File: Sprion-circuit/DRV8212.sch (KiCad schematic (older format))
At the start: 19 parts, among them U1 LM358, U2 LM358

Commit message: デスクトップいくよーーー
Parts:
- removed U1, U2: LM358, symbol Amplifier_Operational:LM358
- added C14: 0.1u, symbol Device:C
- added IC3, IC4: AD8601, symbol Sprion-circuit:AD8601
- C3: value 0.1 -> 0.1u
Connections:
- wire segments 45 -> 42
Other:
- moved on the sheet: C1, C2, R1, R2, R4, R5

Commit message: Push, Push, Push
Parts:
- C1, C2: value 0.1 -> 0.1u
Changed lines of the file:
@@
 	0    1    1    0
 $EndComp
-Text HLabel 3800 1950 2    50   Input ~ 0
+Text HLabel 3800 1950 2    50   Output ~ 0
 MD1_OUT1
-Text HLabel 3800 2250 2    50   Input ~ 0
+Text HLabel 3800 2250 2    50   Output ~ 0
 MD1_OUT2
 $Comp
@@
 	1    0    0    -1
 $EndComp
-Text HLabel 4850 3200 2    50   Input ~ 0
+Text HLabel 4850 3200 2    50   Output ~ 0
 MD1_CS
 $Comp
@@
 P 4300 4300
 F 0 "C1" V 4048 4300 50  0000 C CNN
-F 1 "0.1" V 4139 4300 50  0000 C CNN
+F 1 "0.1u" V 4139 4300 50  0000 C CNN
 F 2 "" H 4338 4150 50  0001 C CNN
 F 3 "~" H 4300 4300 50  0001 C CNN
@@
 	0    1    1    0
 $EndComp
-Text HLabel 3800 4700 2    50   Input ~ 0
+Text HLabel 3800 4700 2    50   Output ~ 0
 MD2_OUT1
-Text HLabel 3800 5000 2    50   Input ~ 0
+Text HLabel 3800 5000 2    50   Output ~ 0
 MD2_OUT2
 $Comp
@@
 	1    0    0    -1
 $EndComp
-Text HLabel 4850 5950 2    50   Input ~ 0
+Text HLabel 4850 5950 2    50   Output ~ 0
 MD2_CS
 $Comp
@@
 P 4300 7050
 F 0 "C2" V 4048 7050 50  0000 C CNN
-F 1 "0.1" V 4139 7050 50  0000 C CNN
+F 1 "0.1u" V 4139 7050 50  0000 C CNN
 F 2 "" H 4338 6900 50  0001 C CNN
 F 3 "~" H 4300 7050 50  0001 C CNN
@@
 	0    1    1    0
 $EndComp
-Text HLabel 8350 1950 2    50   Input ~ 0
+Text HLabel 8350 1950 2    50   Output ~ 0
 MD_SUC_OUT1
-Text HLabel 8350 2250 2    50   Input ~ 0
+Text HLabel 8350 2250 2    50   Output ~ 0
 MD_SUC_OUT2
 $Comp

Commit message: :fix　いろいろ
後で書きます
とりあえず寝ます
許してください
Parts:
- added J?: Conn_01x02_Female, symbol Connector:Conn_01x02_Female
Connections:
- net MD_SUC_OUT1: no longer names the net of MD3.6 (OUT1)
- net MD_SUC_OUT1: now also J?.1 (Pin_1)
- net MD_SUC_OUT2: no longer names the net of MD3.4 (OUT2)
- net MD_SUC_OUT2: now also J?.2 (Pin_2)
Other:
- moved on the sheet: C6, MD3
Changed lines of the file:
@@
 $Descr A4 11693 8268
 encoding utf-8
-Sheet 2 5
+Sheet 2 6
 Title ""
 Date ""
@@
 Wire Wire Line
 	3900 4000 3900 4300
-Text Notes 5600 3550 0    50   ~ 0
-Amplification rate:51\nTransfer function:V_out=0.51*I_s\nCut off frequency:796Hz
 $Comp
 L Sprion-circuit:DRV8212_DRL MD2
@@
 	3900 6750 3900 7050
 $Comp
-L Sprion-circuit:DRV8212_DRL MD3
-U 1 1 60F210D1
-P 8000 2100
-F 0 "MD3" H 8000 2515 50  0000 C CNN
-F 1 "DRV8212_DRL" H 8000 2424 50  0000 C CNN
-F 2 "" H 8000 2100 50  0001 C CNN
-F 3 "" H 8000 2100 50  0001 C CNN
-	1    8000 2100
-	1    0    0    -1
-$EndComp
-Text HLabel 7650 1950 0    50   Input ~ 0
-MD_SUC_IN1
-Text HLabel 7650 2100 0    50   Input ~ 0
-MD_SUC_IN2
-$Comp
 L power:+BATT #PWR0112
 U 1 1 60F210D9
-P 9200 2100
-F 0 "#PWR0112" H 9200 1950 50  0001 C CNN
-F 1 "+BATT" V 9215 2228 50  0000 L CNN
-F 2 "" H 9200 2100 50  0001 C CNN
-F 3 "" H 9200 2100 50  0001 C CNN
-	1    9200 2100
-	0    1    1    0
-$EndComp
-Text HLabel 8350 1950 2    50   Output ~ 0
-MD_SUC_OUT1
-Text HLabel 8350 2250 2    50   Output ~ 0
-MD_SUC_OUT2
+P 8350 1600
+F 0 "#PWR0112" H 8350 1450 50  0001 C CNN
+F 1 "+BATT" V 8365 1728 50  0000 L CNN
+F 2 "" H 8350 1600 50  0001 C CNN
+F 3 "" H 8350 1600 50  0001 C CNN
+	1    8350 1600
+	1    0    0    -1
+$EndComp
 $Comp
 L power:GND #PWR0113
 U 1 1 60F210E1
-P 8950 2400
-F 0 "#PWR0113" H 8950 2150 50  0001 C CNN
-F 1 "GND" H 8955 2227 50  0000 C CNN
-F 2 "" H 8950 2400 50  0001 C CNN
-F 3 "" H 8950 2400 50  0001 C CNN
-	1    8950 2400
-	1    0    0    -1
-$EndComp
-$Comp
-L Device:C C6
-U 1 1 60F210E7
-P 8950 2250
-F 0 "C6" H 9065 2296 50  0000 L CNN
-F 1 "0.1u" H 9065 2205 50  0000 L CNN
-F 2 "" H 8988 2100 50  0001 C CNN
-F 3 "~" H 8950 2250 50  0001 C CNN
-	1    8950 2250
-	1    0    0    -1
-$EndComp
-Wire Wire Line
-	8350 2100 8950 2100
-Connection ~ 8950 2100
-Wire Wire Line
-	8950 2100 9200 2100
-$Comp
-L power:GND #PWR0114
-U 1 1 60F21B92
-P 7650 2250
-F 0 "#PWR0114" H 7650 2000 50  0001 C CNN
-F 1 "GND" H 7655 2077 50  0000 C CNN
-F 2 "" H 7650 2250 50  0001 C CNN
-F 3 "" H 7650 2250 50  0001 C CNN
-	1    7650 2250
+P 8950 1850
+F 0 "#PWR0113" H 8950 1600 50  0001 C CNN
+F 1 "GND" H 8955 1677 50  0000 C CNN
+F 2 "" H 8950 1850 50  0001 C CNN
+F 3 "" H 8950 1850 50  0001 C CNN
+	1    8950 1850
 	1    0    0    -1
 $EndComp
@@
 	4200 5650 4350 5650
 Connection ~ 4200 5650
+$Comp
+L power:GND #PWR0114
+U 1 1 60F21B92
+P 7450 2600
+F 0 "#PWR0114" H 7450 2350 50  0001 C CNN
+F 1 "GND" H 7455 2427 50  0000 C CNN
+F 2 "" H 7450 2600 50  0001 C CNN
+F 3 "" H 7450 2600 50  0001 C CNN
+	1    7450 2600
+	1    0    0    -1
+$EndComp
+Text HLabel 7450 2450 0    50   Input ~ 0
+MD_SUC_IN2
+Text HLabel 7450 2300 0    50   Input ~ 0
+MD_SUC_IN1
+$Comp
+L Sprion-circuit:DRV8212_DRL MD3
+U 1 1 60F210D1
+P 7800 2450
+F 0 "MD3" H 7800 2865 50  0000 C CNN
+F 1 "DRV8212_DRL" H 7800 2774 50  0000 C CNN
+F 2 "" H 7800 2450 50  0001 C CNN
+F 3 "" H 7800 2450 50  0001 C CNN
+	1    7800 2450
+	1    0    0    -1
+$EndComp
+Text Notes 5600 3550 0    50   ~ 0
+Amplification rate:51\nTransfer function:V_out=0.51*I_s\nCut off frequency:796Hz
+$Comp
+L Connector:Conn_01x02_Female J?
+U 1 1 61A82ABA
+P 10000 2300
+F 0 "J?" H 10028 2276 50  0000 L CNN
+F 1 "Conn_01x02_Female" H 10028 2185 50  0000 L CNN
+F 2 "" H 10000 2300 50  0001 C CNN
+F 3 "~" H 10000 2300 50  0001 C CNN
+	1    10000 2300
+	1    0    0    -1
+$EndComp
+Wire Wire Line
+	8150 2300 9800 2300
+Wire Wire Line
+	8150 2600 9800 2600
+Wire Wire Line
+	9800 2600 9800 2400
+Wire Wire Line
+	8350 2450 8150 2450
+Wire Wire Line
+	8350 1600 8350 1850
+$Comp
+L Device:C C6
+U 1 1 60F210E7
+P 8700 1850
+F 0 "C6" H 8815 1896 50  0000 L CNN
+F 1 "0.1u" H 8815 1805 50  0000 L CNN
+F 2 "" H 8738 1700 50  0001 C CNN
+F 3 "~" H 8700 1850 50  0001 C CNN
+	1    8700 1850
+	0    -1   -1   0
+$EndComp
+Wire Wire Line
+	8550 1850 8350 1850
+Connection ~ 8350 1850
+Wire Wire Line
+	8350 1850 8350 2450
+Wire Wire Line
+	8850 1850 8950 1850
 $EndSCHEMATC

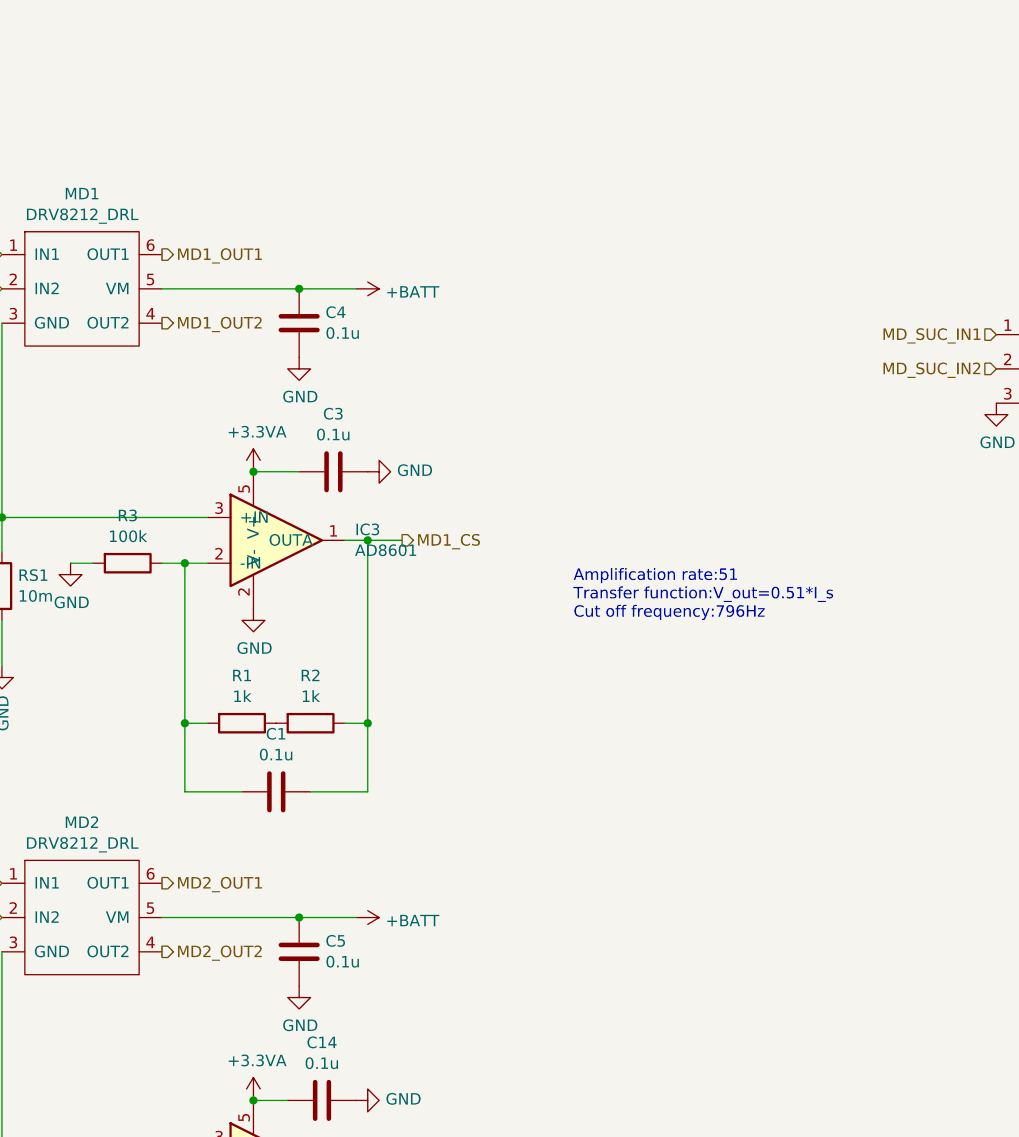
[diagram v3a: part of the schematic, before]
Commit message: fix: MD周り,タイマー割り当て
MDの書き方を変えた
タイマー割り当てを再構成、対称性・高性能タイマーをどうするかみたいなとこ
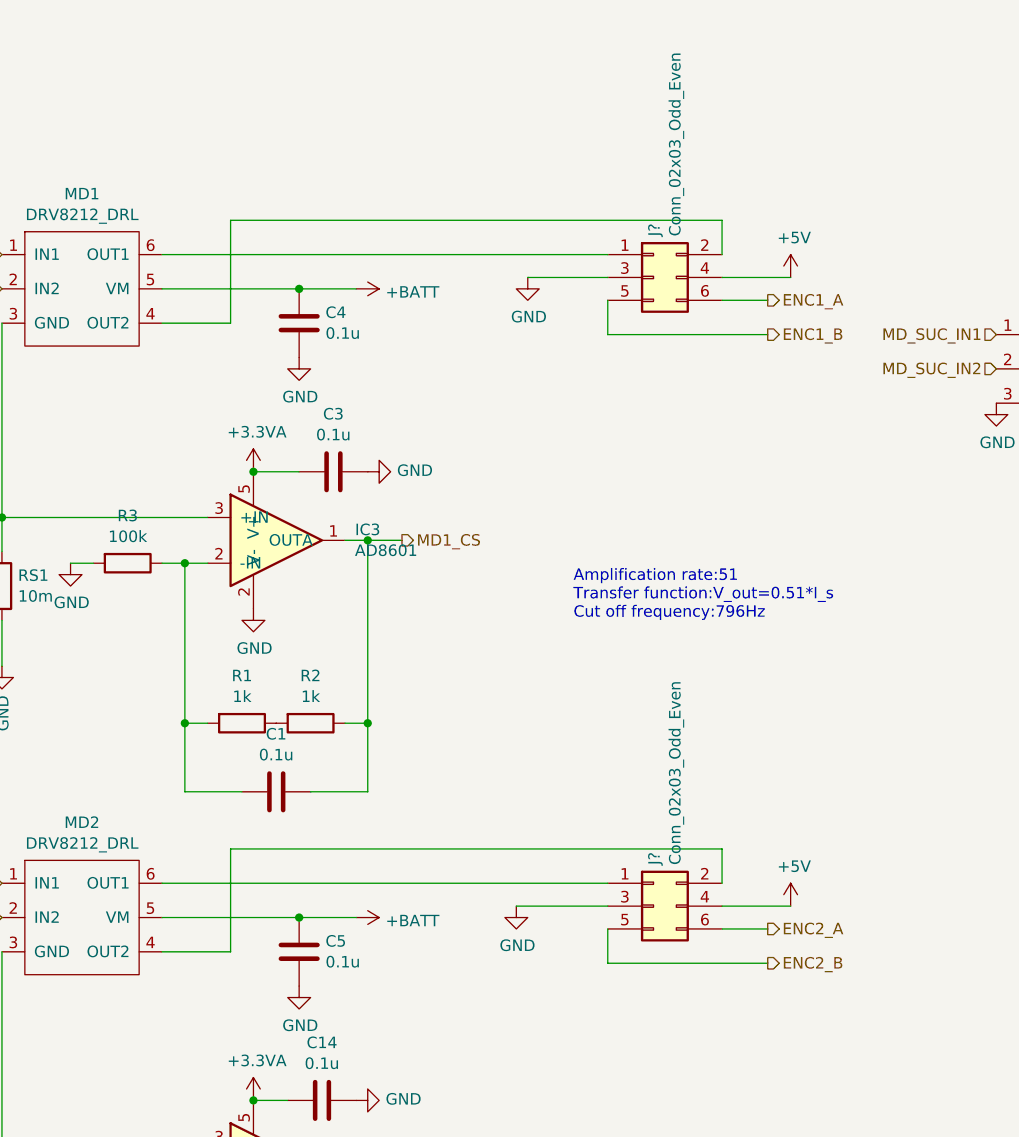
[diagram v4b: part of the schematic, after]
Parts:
- added J? (x2): Conn_02x03_Odd_Even, symbol Connector_Generic:Conn_02x03_Odd_Even
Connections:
- net GND: now also J?.3 (Pin_3), J?.3 (Pin_3)
- net MD1_OUT1: no longer names the net of MD1.6 (OUT1)
- net MD1_OUT1: now also J?.1 (Pin_1)
- net MD1_OUT2: no longer names the net of MD1.4 (OUT2)
- net MD1_OUT2: now also J?.2 (Pin_2)
- net MD2_OUT1: no longer names the net of MD2.6 (OUT1)
- net MD2_OUT1: now also J?.1 (Pin_1)
- net MD2_OUT2: no longer names the net of MD2.4 (OUT2)
- net MD2_OUT2: now also J?.2 (Pin_2)
- new net +5V: J?.4 (Pin_4), J?.4 (Pin_4)
- new net ENC1_A: J?.6 (Pin_6)
- new net ENC1_B: J?.5 (Pin_5)
- new net ENC2_A: J?.6 (Pin_6)
- new net ENC2_B: J?.5 (Pin_5)

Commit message: add,feat,fix:すまんコミットわすれててぐちゃぐちゃや
配置始めた。
フットプリント割り当てた
回路図pdfで吐いた
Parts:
- removed C14, C3: 0.1u, symbol Device:C
- removed IC3, IC4: AD8601, symbol Sprion-circuit:AD8601
- removed R1, R2, R4, R5: 1k, symbol Device:R
- removed R3, R6: 100k, symbol Device:R
- added U2, U5: INA185, Package_TO_SOT_SMD:SOT-563, symbol Amplifier_Current:INA181
- C1, C2, C4, C5, C6: footprint (none) -> Capacitor_SMD:C_0603_1608Metric
- J3, J4: renamed from J?; footprint (none) -> Connector_IDC:IDC-Header_2x03_P2.54mm_Vertical
- J5: renamed from J?; footprint (none) -> Connector_PinHeader_2.54mm:PinHeader_1x02_P2.54mm_Vertical
- MD1, MD2, MD3: footprint (none) -> Package_TO_SOT_SMD:SOT-563
- RS1, RS2: value 10m -> 3m; footprint (none) -> Resistor_SMD:R_0805_2012Metric
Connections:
- net +3.3VA: now also C1.1, C2.1, U2.6 (V+), U5.6 (V+)
- net GND: now also C1.2, C2.2, MD1.3 (GND), MD2.3 (GND), U2.2 (GND), U5.2 (GND); no longer RS1.2, RS2.2
- net MD1_CS: now also U2.1; no longer C1.1
- net MD2_CS: now also U5.1; no longer C2.1
- net at RS1.1: now also MD1.4 (OUT2), U2.3 (+); no longer MD1.3 (GND)
- net at J3.2 (Pin_2): now also RS1.2, U2.4 (-); no longer MD1.4 (OUT2)
- net at RS2.1: now also MD2.4 (OUT2), U5.3 (+); no longer MD2.3 (GND)
- net at J4.2 (Pin_2): now also RS2.2, U5.4 (-); no longer MD2.4 (OUT2)
- new net VREF: U2.5 (REF), U5.5 (REF)
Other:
- note added: "Gain:100\n"
- note removed: "Amplification rate:51\nTransfer function:V_out=0.51*I_s\nCut off frequency:796Hz"
- moved on the sheet: C5, J4, MD2

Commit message: add fix feat: でけたー（コミットしてなくてごめん）
ベタ塗、配線、再配置等
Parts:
- MD1, MD2, MD3, U2, U5: footprint Package_TO_SOT_SMD:SOT-563 -> Sprion-circuit:SOT-563
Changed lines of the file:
@@
 $Descr A4 11693 8268
 encoding utf-8
-Sheet 6 6
+Sheet 5 6
 Title ""
 Date ""
@@
 F 0 "MD1" H 3450 2515 50  0000 C CNN
 F 1 "DRV8212_DRL" H 3450 2424 50  0000 C CNN
-F 2 "Package_TO_SOT_SMD:SOT-563" H 3450 2100 50  0001 C CNN
+F 2 "Sprion-circuit:SOT-563" H 3450 2100 50  0001 C CNN
 F 3 "" H 3450 2100 50  0001 C CNN
 	1    3450 2100
@@
 F 0 "MD2" H 3450 5715 50  0000 C CNN
 F 1 "DRV8212_DRL" H 3450 5624 50  0000 C CNN
-F 2 "Package_TO_SOT_SMD:SOT-563" H 3450 5300 50  0001 C CNN
+F 2 "Sprion-circuit:SOT-563" H 3450 5300 50  0001 C CNN
 F 3 "" H 3450 5300 50  0001 C CNN
 	1    3450 5300
@@
 F 0 "MD3" H 7800 2865 50  0000 C CNN
 F 1 "DRV8212_DRL" H 7800 2774 50  0000 C CNN
-F 2 "Package_TO_SOT_SMD:SOT-563" H 7800 2450 50  0001 C CNN
+F 2 "Sprion-circuit:SOT-563" H 7800 2450 50  0001 C CNN
 F 3 "" H 7800 2450 50  0001 C CNN
 	1    7800 2450
@@
 F 0 "U2" H 4894 3296 50  0000 L CNN
 F 1 "INA185" H 4894 3205 50  0000 L CNN
-F 2 "Package_TO_SOT_SMD:SOT-563" H 4600 3300 50  0001 C CNN
+F 2 "Sprion-circuit:SOT-563" H 4600 3300 50  0001 C CNN
 F 3 "http://www.ti.com/lit/ds/symlink/ina181.pdf" H 4700 3400 50  0001 C CNN
 	1    4550 3250
@@
 F 0 "U5" H 4894 6496 50  0000 L CNN
 F 1 "INA185" H 4894 6405 50  0000 L CNN
-F 2 "Package_TO_SOT_SMD:SOT-563" H 4600 6500 50  0001 C CNN
+F 2 "Sprion-circuit:SOT-563" H 4600 6500 50  0001 C CNN
 F 3 "http://www.ti.com/lit/ds/symlink/ina181.pdf" H 4700 6600 50  0001 C CNN
 	1    4550 6450
